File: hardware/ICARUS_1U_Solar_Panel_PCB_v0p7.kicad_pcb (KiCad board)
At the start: 2 copper layers, 95 x 95 mm, 11 parts, among them J1 Molex_53398-0471

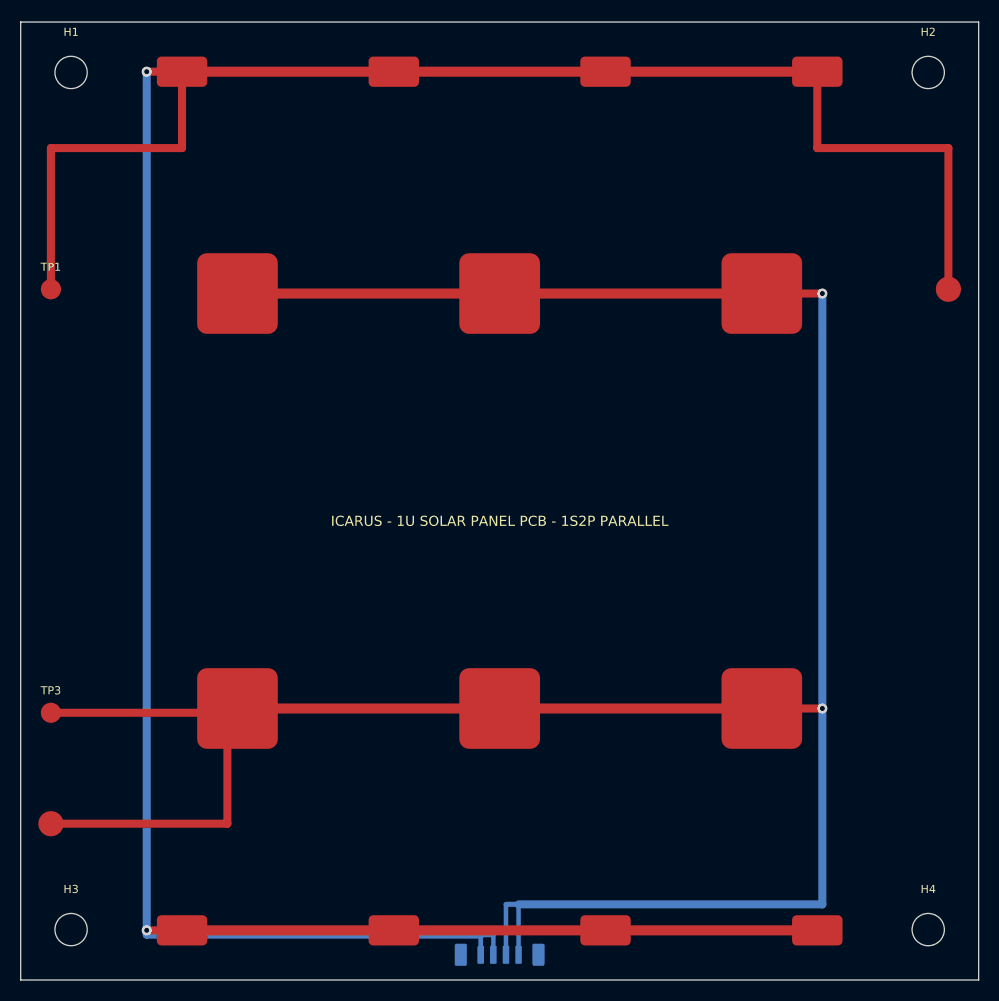
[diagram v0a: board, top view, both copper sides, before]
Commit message: Sync TP and MountingHole footprints with KiCad 10 stdlib (zeros 10 warnings)
Manually rewrote the 8 embedded footprints (TP1, TP3, TP4, TP5 +
H1-H4) to match the structure of the standard KiCad 10.0 library
versions in
  C:\Program Files\KiCad\10.0\share\kicad\footprints\TestPoint.pretty
  C:\Program Files\KiCad\10.0\share\kicad\footprints\MountingHole.pretty
preserving the instance-specific bits (uuid, position, reference,
pad net assignments).

Schematic: set TP1 and TP3 to in_bom=no to match the stdlib
TestPoint_Pad_D2.0mm attr exclude_from_bom (test pads are not
purchasable components — they are built into the PCB).

DRC result:
- v0.6: 13 warnings (3 lib + 10 lib_mismatch)
- v0.7 before this commit: 11 warnings (D1 + TP2 already removed)
- v0.7 now: 3 warnings (only lib_footprint_issues from CLI not
  resolving ICARUS_Solar / ICARUS_Connector local libs).

All 10 lib_footprint_mismatch warnings cleared.

Co-Authored-By: Claude Opus 4.7 <noreply@anthropic.com>
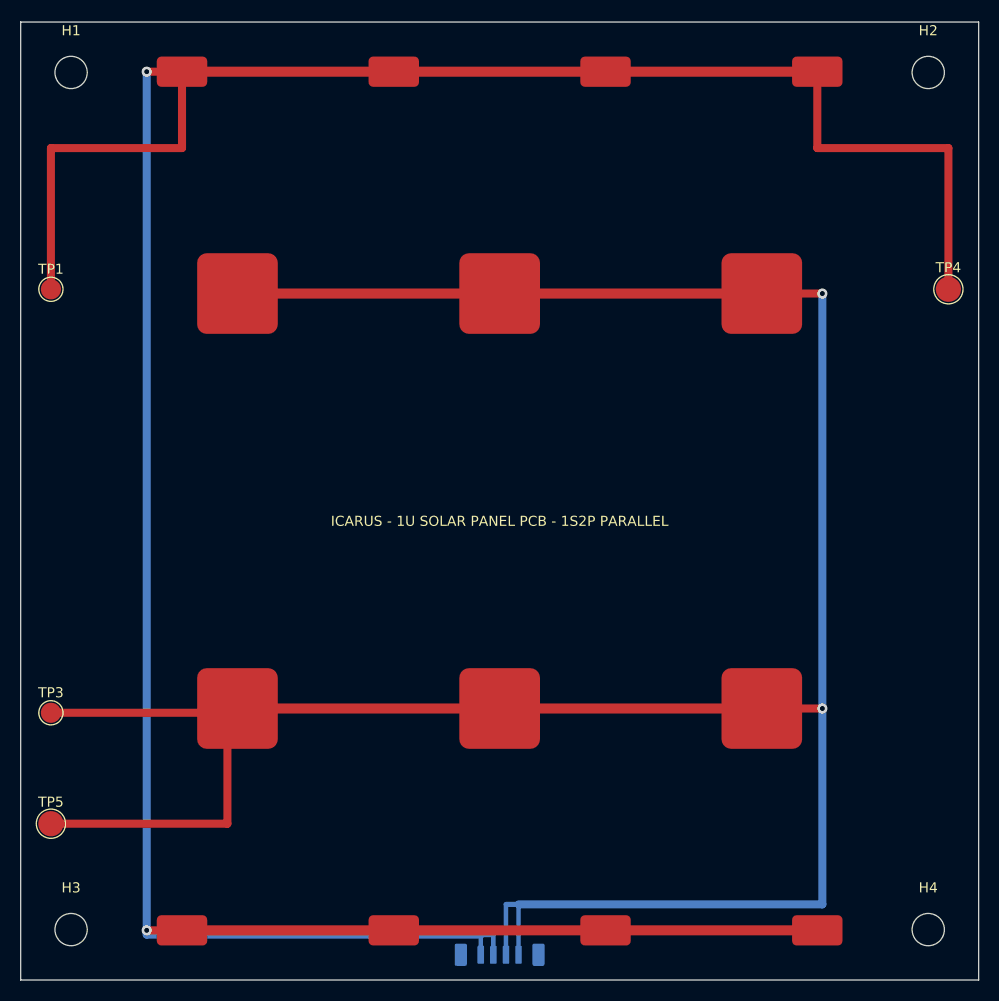
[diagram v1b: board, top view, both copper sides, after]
